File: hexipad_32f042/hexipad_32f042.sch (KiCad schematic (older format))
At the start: 35 parts, among them J1 PGM, J10 MNT, J11 MNT, J12 MNT, J13 MNT, J14 ARTWORK, J15 ARTWORK, J2 USB_B_Micro, J3 PORTB, J4 PORTA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

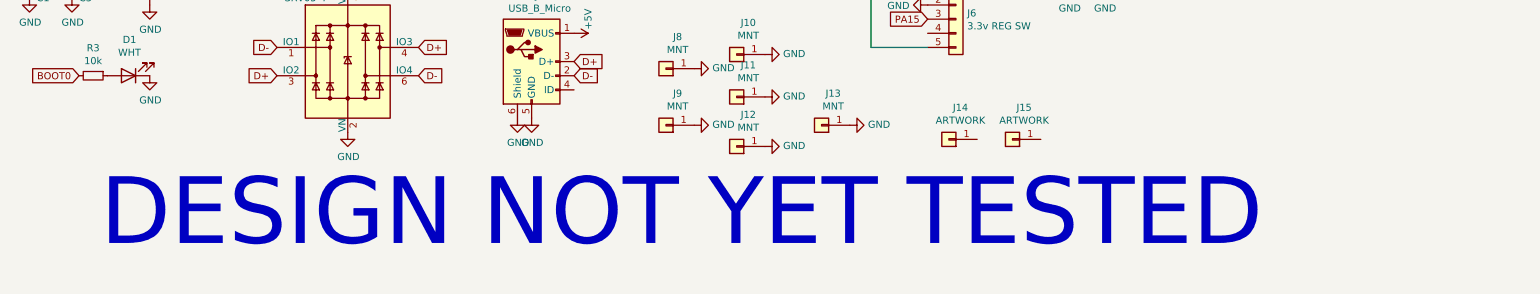
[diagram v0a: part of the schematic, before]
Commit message: bump revision and rename our breakout to hexipad.
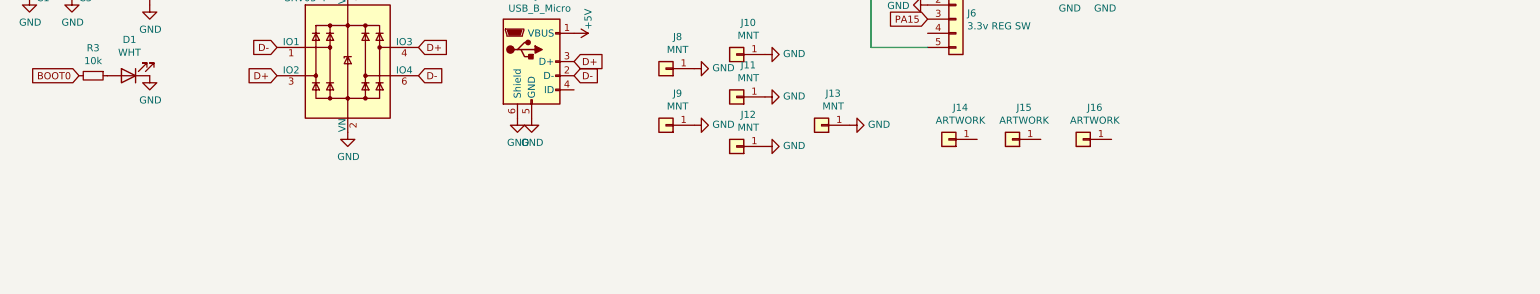
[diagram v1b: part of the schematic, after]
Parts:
- added J16: ARTWORK, stm32f042_breakout:cb-signature, symbol Connector_Generic:Conn_01x01
- J1: footprint POGO-5:POGO-5 -> stlink-pgmhdr:POGO-5
- J2: footprint Connector_USB:USB_Micro-B_GCT_USB3076-30-A -> chinese_connectors:chinausb-multi
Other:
- note removed: "DESIGN NOT YET TESTED"
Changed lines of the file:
@@
 F 0 "J1" H 668 2125 50  0000 C CNN
 F 1 "PGM" H 668 2216 50  0000 C CNN
-F 2 "POGO-5:POGO-5" H 750 2550 50  0001 C CNN
+F 2 "stlink-pgmhdr:POGO-5" H 750 2550 50  0001 C CNN
 F 3 "~" H 750 2550 50  0001 C CNN
 F 4 "DNP" H 750 2550 50  0001 C CNN "DNP"
@@
 F 0 "J2" H 4357 4417 50  0000 C CNN
 F 1 "USB_B_Micro" H 4357 4326 50  0000 C CNN
-F 2 "Connector_USB:USB_Micro-B_GCT_USB3076-30-A" H 4450 3900 50  0001 C CNN
+F 2 "chinese_connectors:chinausb-multi" H 4450 3900 50  0001 C CNN
 F 3 "~" H 4450 3900 50  0001 C CNN
 F 4 ".0407" H 4300 3950 50  0001 C CNN "Cost100"
@@
 	0    -1   -1   0
 $EndComp
-Text Notes 1250 5300 0    472  ~ 0
-DESIGN NOT YET TESTED
 $Comp
 L Connector_Generic:Conn_02x09_Odd_Even J3
@@
 	-1   0    0    1
 $EndComp
+$Comp
+L Connector_Generic:Conn_01x01 J16
+U 1 1 5F1E7A36
+P 8200 4500
+F 0 "J16" H 8118 4275 50  0000 C CNN
+F 1 "ARTWORK" H 8118 4366 50  0000 C CNN
+F 2 "stm32f042_breakout:cb-signature" H 8200 4500 50  0001 C CNN
+F 3 "~" H 8200 4500 50  0001 C CNN
+	1    8200 4500
+	-1   0    0    1
+$EndComp

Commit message: Correct part #
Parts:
- J2: LCSC https://lcsc.com/product-detail/USB-Connectors_Jing-Extension-of-the-Electronic-Co-Jing-Extension-of-the-Electronic-Co-micro-5PBoard5-9No-column-plus-welding-feet-High-temperature_C40955.html -> https://lcsc.com/product-detail/USB-Connectors_Jing-Extension-of-the-Electronic-Co-C40953_C40953.html
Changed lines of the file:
@@
 F 3 "~" H 4450 3900 50  0001 C CNN
 F 4 ".0407" H 4300 3950 50  0001 C CNN "Cost100"
-F 5 "https://lcsc.com/product-detail/USB-Connectors_Jing-Extension-of-the-Electronic-Co-Jing-Extension-of-the-Electronic-Co-micro-5PBoard5-9No-column-plus-welding-feet-High-temperature_C40955.html" H 4300 3950 50  0001 C CNN "LCSC"
+F 5 "https://lcsc.com/product-detail/USB-Connectors_Jing-Extension-of-the-Electronic-Co-C40953_C40953.html" H 4300 3950 50  0001 C CNN "LCSC"
 	1    4300 3950
 	1    0    0    -1

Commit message: various updates
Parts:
- C1, C2, C3, C4, C5, C6, C7, C8, C9: symbol Device:C_Small -> hexipad_32f042-rescue:C_Small-Device
- D1: symbol Device:LED -> hexipad_32f042-rescue:LED-Device
- J1, J6: symbol Connector_Generic:Conn_01x05 -> hexipad_32f042-rescue:Conn_01x05-Connector_Generic
- J10, J11, J12, J13, J14, J15, J16, J8, J9: symbol Connector_Generic:Conn_01x01 -> hexipad_32f042-rescue:Conn_01x01-Connector_Generic
- J2: symbol Connector:USB_B_Micro -> hexipad_32f042-rescue:USB_B_Micro-Connector
- J3, J4: symbol Connector_Generic:Conn_02x09_Odd_Even -> hexipad_32f042-rescue:Conn_02x09_Odd_Even-Connector_Generic
- J5: symbol Connector_Generic:Conn_02x05_Odd_Even -> hexipad_32f042-rescue:Conn_02x05_Odd_Even-Connector_Generic
- J7: symbol Connector:Micro_SD_Card_Det -> hexipad_32f042-rescue:Micro_SD_Card_Det-Connector
- JP1: symbol Jumper:SolderJumper_2_Bridged -> hexipad_32f042-rescue:SolderJumper_2_Bridged-Jumper
- R1, R2, R3: symbol Device:R_Small -> hexipad_32f042-rescue:R_Small-Device
- SW1, SW2: symbol Switch:SW_Push_45deg -> hexipad_32f042-rescue:SW_Push_45deg-Switch
- U1: symbol Regulator_Linear:AP1117-33 -> hexipad_32f042-rescue:AP1117-33-Regulator_Linear
- U2: symbol Power_Protection:SRV05-4 -> hexipad_32f042-rescue:SRV05-4-Power_Protection
- U3: symbol MCU_ST_STM32F0:STM32F042G4Ux -> hexipad_32f042-rescue:STM32F042G4Ux-MCU_ST_STM32F0
- Y1: symbol Device:Crystal_GND24_Small -> hexipad_32f042-rescue:Crystal_GND24_Small-Device

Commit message: add rev B - fix USB
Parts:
- C1, C2, C3, C4, C5, C6, C7, C8, C9: symbol hexipad_32f042-rescue:C_Small-Device -> hexipad_32f042-rescue:C_Small-Device-hexipad_32f042-rescue
- D1: symbol hexipad_32f042-rescue:LED-Device -> hexipad_32f042-rescue:LED-Device-hexipad_32f042-rescue
- J1, J6: symbol hexipad_32f042-rescue:Conn_01x05-Connector_Generic -> hexipad_32f042-rescue:Conn_01x05-Connector_Generic-hexipad_32f042-rescue
- J10, J11, J12, J13, J14, J15, J16, J8, J9: symbol hexipad_32f042-rescue:Conn_01x01-Connector_Generic -> hexipad_32f042-rescue:Conn_01x01-Connector_Generic-hexipad_32f042-rescue
- J2: footprint chinese_connectors:chinausb-multi -> chinese-connectors:chinausb-multi; symbol hexipad_32f042-rescue:USB_B_Micro-Connector -> hexipad_32f042-rescue:USB_B_Micro-Connector-hexipad_32f042-rescue
- J3, J4: symbol hexipad_32f042-rescue:Conn_02x09_Odd_Even-Connector_Generic -> hexipad_32f042-rescue:Conn_02x09_Odd_Even-Connector_Generic-hexipad_32f042-rescue
- J5: symbol hexipad_32f042-rescue:Conn_02x05_Odd_Even-Connector_Generic -> hexipad_32f042-rescue:Conn_02x05_Odd_Even-Connector_Generic-hexipad_32f042-rescue
- J7: symbol hexipad_32f042-rescue:Micro_SD_Card_Det-Connector -> hexipad_32f042-rescue:Micro_SD_Card_Det-Connector-hexipad_32f042-rescue
- JP1: symbol hexipad_32f042-rescue:SolderJumper_2_Bridged-Jumper -> hexipad_32f042-rescue:SolderJumper_2_Bridged-Jumper-hexipad_32f042-rescue
- R1, R2, R3: symbol hexipad_32f042-rescue:R_Small-Device -> hexipad_32f042-rescue:R_Small-Device-hexipad_32f042-rescue
- SW1, SW2: symbol hexipad_32f042-rescue:SW_Push_45deg-Switch -> hexipad_32f042-rescue:SW_Push_45deg-Switch-hexipad_32f042-rescue
- U1: symbol hexipad_32f042-rescue:AP1117-33-Regulator_Linear -> hexipad_32f042-rescue:AP1117-33-Regulator_Linear-hexipad_32f042-rescue
- U2: symbol hexipad_32f042-rescue:SRV05-4-Power_Protection -> hexipad_32f042-rescue:SRV05-4-Power_Protection-hexipad_32f042-rescue
- U3: symbol hexipad_32f042-rescue:STM32F042G4Ux-MCU_ST_STM32F0 -> hexipad_32f042-rescue:STM32F042G4Ux-MCU_ST_STM32F0-hexipad_32f042-rescue
- Y1: symbol hexipad_32f042-rescue:Crystal_GND24_Small-Device -> hexipad_32f042-rescue:Crystal_GND24_Small-Device-hexipad_32f042-rescue
